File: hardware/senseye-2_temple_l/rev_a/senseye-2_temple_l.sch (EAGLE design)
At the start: 1 part

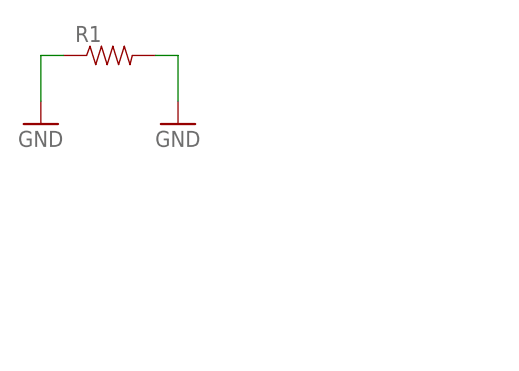
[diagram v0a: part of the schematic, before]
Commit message: moved all to 0,0 origin
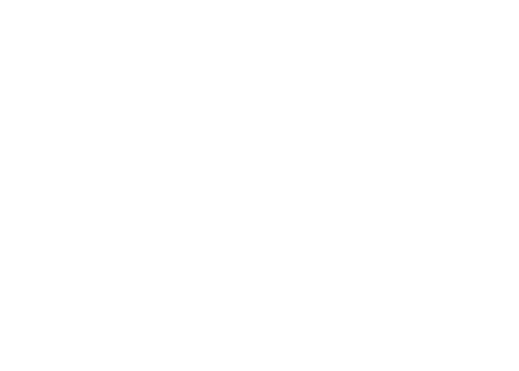
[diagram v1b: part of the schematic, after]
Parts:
- removed R1: (no value), passives:RESISTOR0402_RES
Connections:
- removed net GND: R1.1, R1.2
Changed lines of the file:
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@@
 <parts>
 <part name="FRAME1" library="frames" deviceset="LETTER_L" device=""/>
-<part name="R1" library="passives" deviceset="RESISTOR" device="0402_RES"/>
-<part name="GND1" library="SparkFun-Aesthetics" deviceset="GND" device=""/>
-<part name="GND2" library="SparkFun-Aesthetics" deviceset="GND" device=""/>
 </parts>
 <sheets>
@@
 <instance part="FRAME1" gate="G$1" x="0" y="0"/>
 <instance part="FRAME1" gate="G$2" x="147.32" y="0"/>
-<instance part="R1" gate="G$1" x="127" y="109.22"/>
-<instance part="GND1" gate="1" x="134.62" y="101.6"/>
-<instance part="GND2" gate="1" x="119.38" y="101.6"/>
 </instances>
 <busses>
 </busses>
 <nets>
-<net name="GND" class="0">
-<segment>
-<pinref part="R1" gate="G$1" pin="1"/>
-<pinref part="GND2" gate="1" pin="GND"/>
-<wire x1="121.92" y1="109.22" x2="119.38" y2="109.22" width="0.1524" layer="91"/>
-<wire x1="119.38" y1="109.22" x2="119.38" y2="104.14" width="0.1524" layer="91"/>
-</segment>
-<segment>
-<pinref part="R1" gate="G$1" pin="2"/>
-<pinref part="GND1" gate="1" pin="GND"/>
-<wire x1="132.08" y1="109.22" x2="134.62" y2="109.22" width="0.1524" layer="91"/>
-<wire x1="134.62" y1="109.22" x2="134.62" y2="104.14" width="0.1524" layer="91"/>
-</segment>
-</net>
 </nets>
 </sheet>
